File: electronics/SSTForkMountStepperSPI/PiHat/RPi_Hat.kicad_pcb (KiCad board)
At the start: 4 copper layers, 82 x 69.9 mm, 37 parts, among them CON1 BARREL_JACK, J1 RJ12, J2 RPi_GPIO, J3 RA_STEP, J4 DEC_ENC, J5 RA_ENC, J6 DEC_STEP, Q1 Si2369DS, SW1 SW_SPST, U2 pololu_D24V22F5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

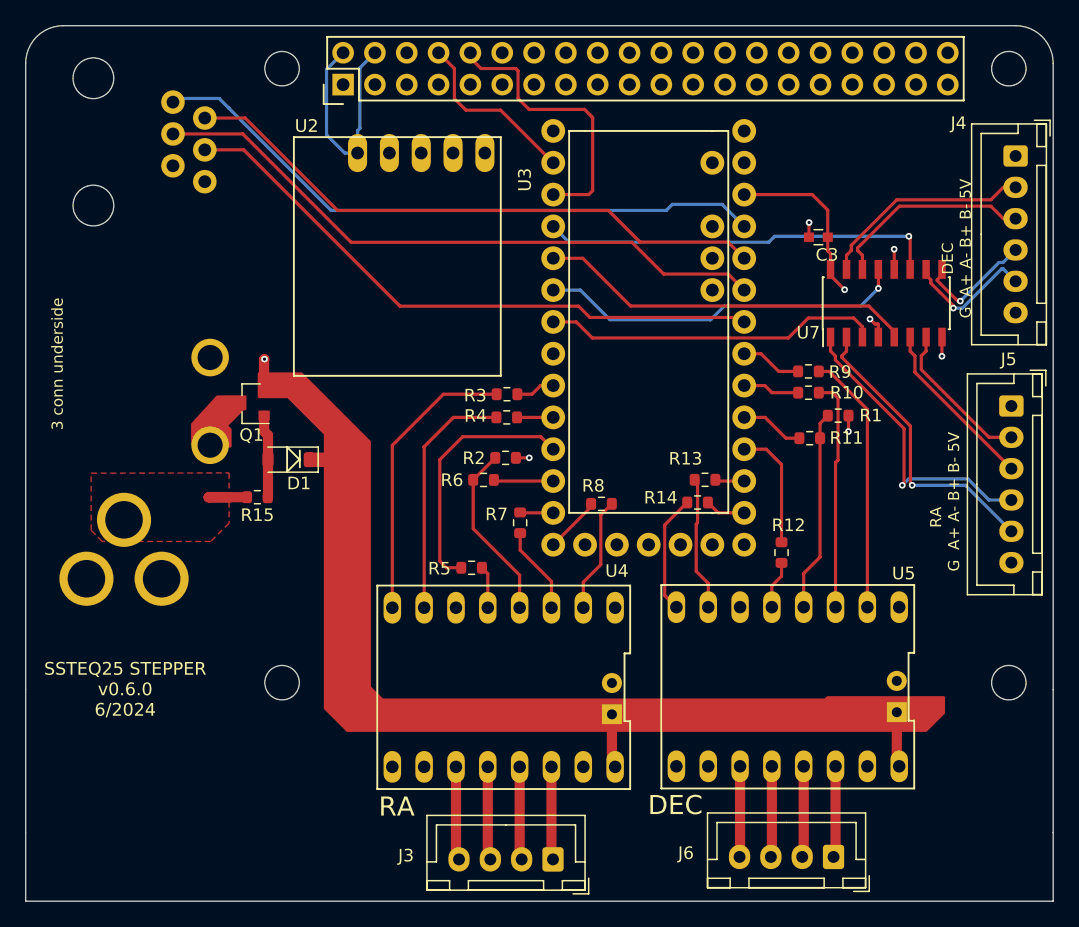
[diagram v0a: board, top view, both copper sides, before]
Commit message: Fixed long commands to micro.
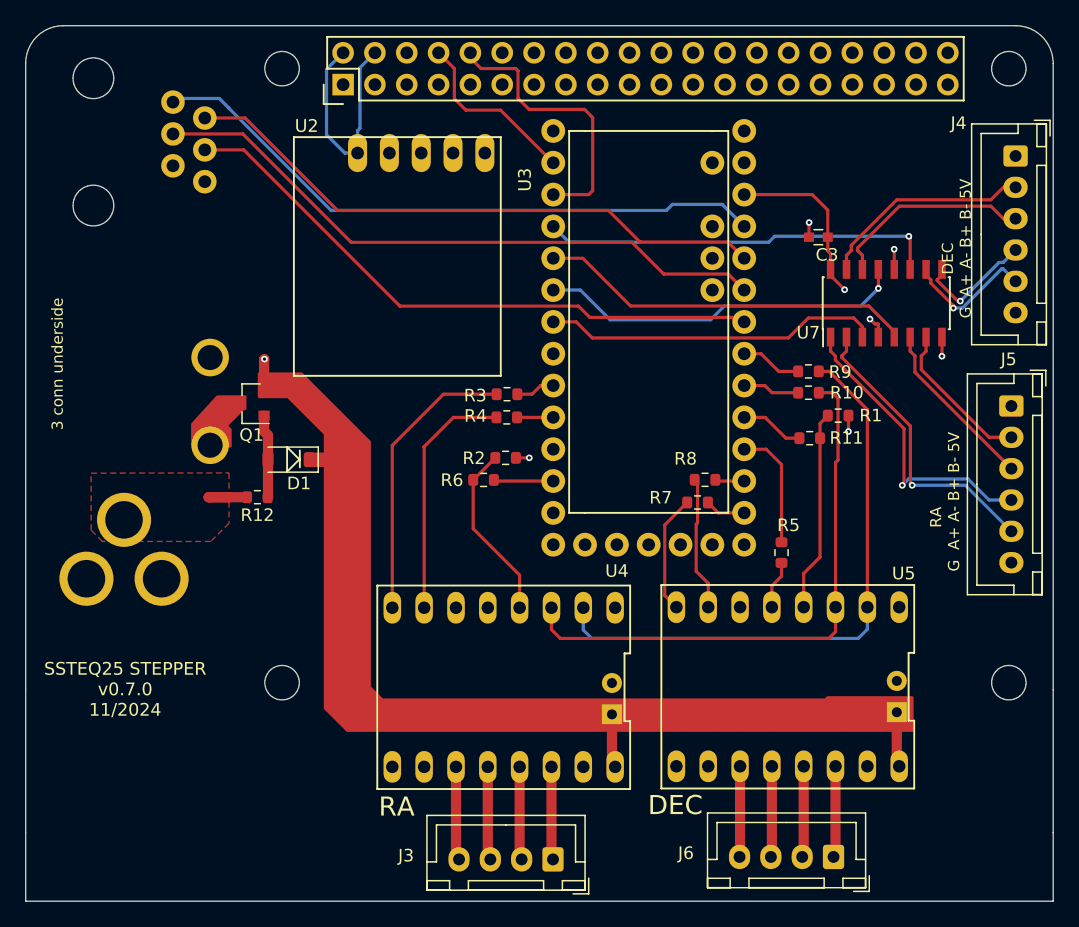
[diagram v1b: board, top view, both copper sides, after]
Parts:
- removed the R5 at (134.4, 109.4)
- removed the R7 at (138.3, 105.8)
- removed the R8 at (144.8, 104.3)
- renumbered R15 to R12, R12 to R5, R14 to R7, R13 to R8
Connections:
- R10 pad 2: DEC_SCK -> SW_SCK
- R5 pad 2: DEC_MISO -> SW_MISO
- R9 pad 2: DEC_MOSI -> SW_MOSI
- U3 pad 11: Net-(U3-11(DOUT)) -> unconnected-(U3-11(DOUT)-Pad11)
- U3 pad 12: Net-(U3-12(DIN)) -> unconnected-(U3-12(DIN)-Pad12)
- U3 pad 9: Net-(U3-9(RX2)) -> unconnected-(U3-9(RX2)-Pad9)
- U4 pad 2: RA_MOSI -> SW_MOSI
- U4 pad 3: RA_SCK -> SW_SCK
- U4 pad 5: RA_MISO -> SW_MISO
- U5 pad 2: DEC_MOSI -> SW_MOSI
- U5 pad 3: DEC_SCK -> SW_SCK
- U5 pad 5: DEC_MISO -> SW_MISO
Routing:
- net SW_MOSI: track 0.00 -> 47.7 mm
- net SW_SCK: track 0.00 -> 45.4 mm
- net SW_MISO: track 0.00 -> 30.7 mm
- net DEC_MOSI: track 20.9 -> 0.00 mm
- net Net-(U3-9(RX2)): track 20.3 -> 0.00 mm
- net DEC_SCK: track 18.5 -> 0.00 mm
- net RA_MOSI: track 9.23 -> 0.00 mm
- net RA_SCK: track 6.99 -> 0.00 mm
- net Net-(U3-12(DIN)): track 4.51 -> 0.00 mm
- net DEC_MISO: track 3.85 -> 0.00 mm
- net RA_MISO: track 3.38 -> 0.00 mm
- net Net-(U3-11(DOUT)): track 2.65 -> 0.00 mm
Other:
- board text added: "SSTEQ25 STEPPER v0.7.0 11/2024"
- board text removed: "SSTEQ25 STEPPER v0.6.0 6/2024"
